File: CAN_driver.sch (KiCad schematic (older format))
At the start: 12 parts, among them J4 DB9_Female, U3 ADM3053

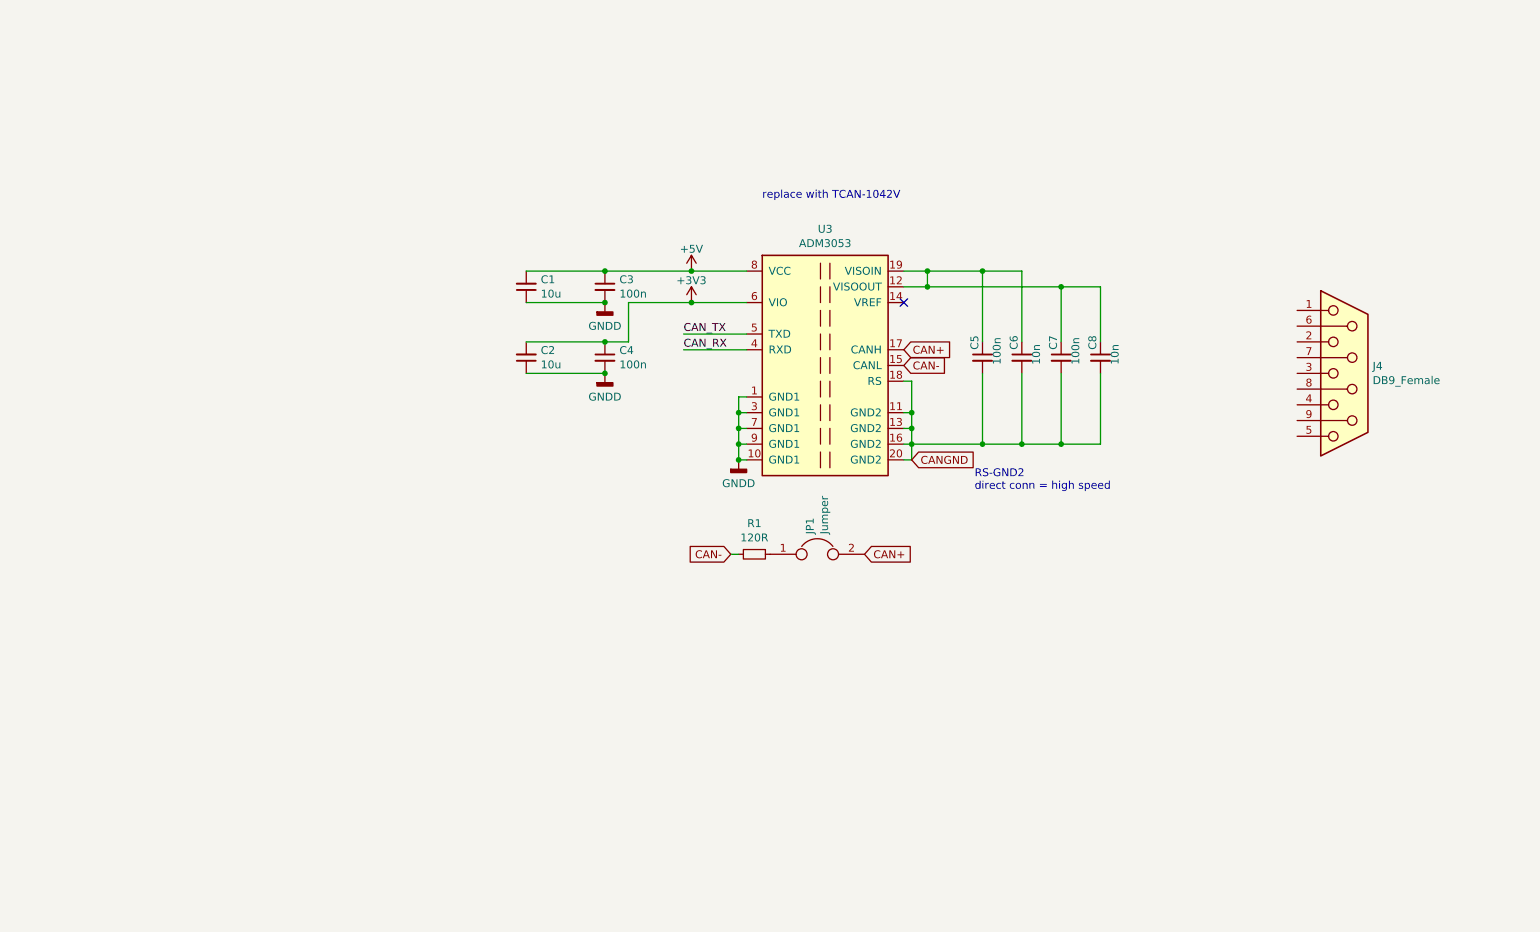
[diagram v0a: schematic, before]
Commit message: added vcu pinout, still lots needs doing
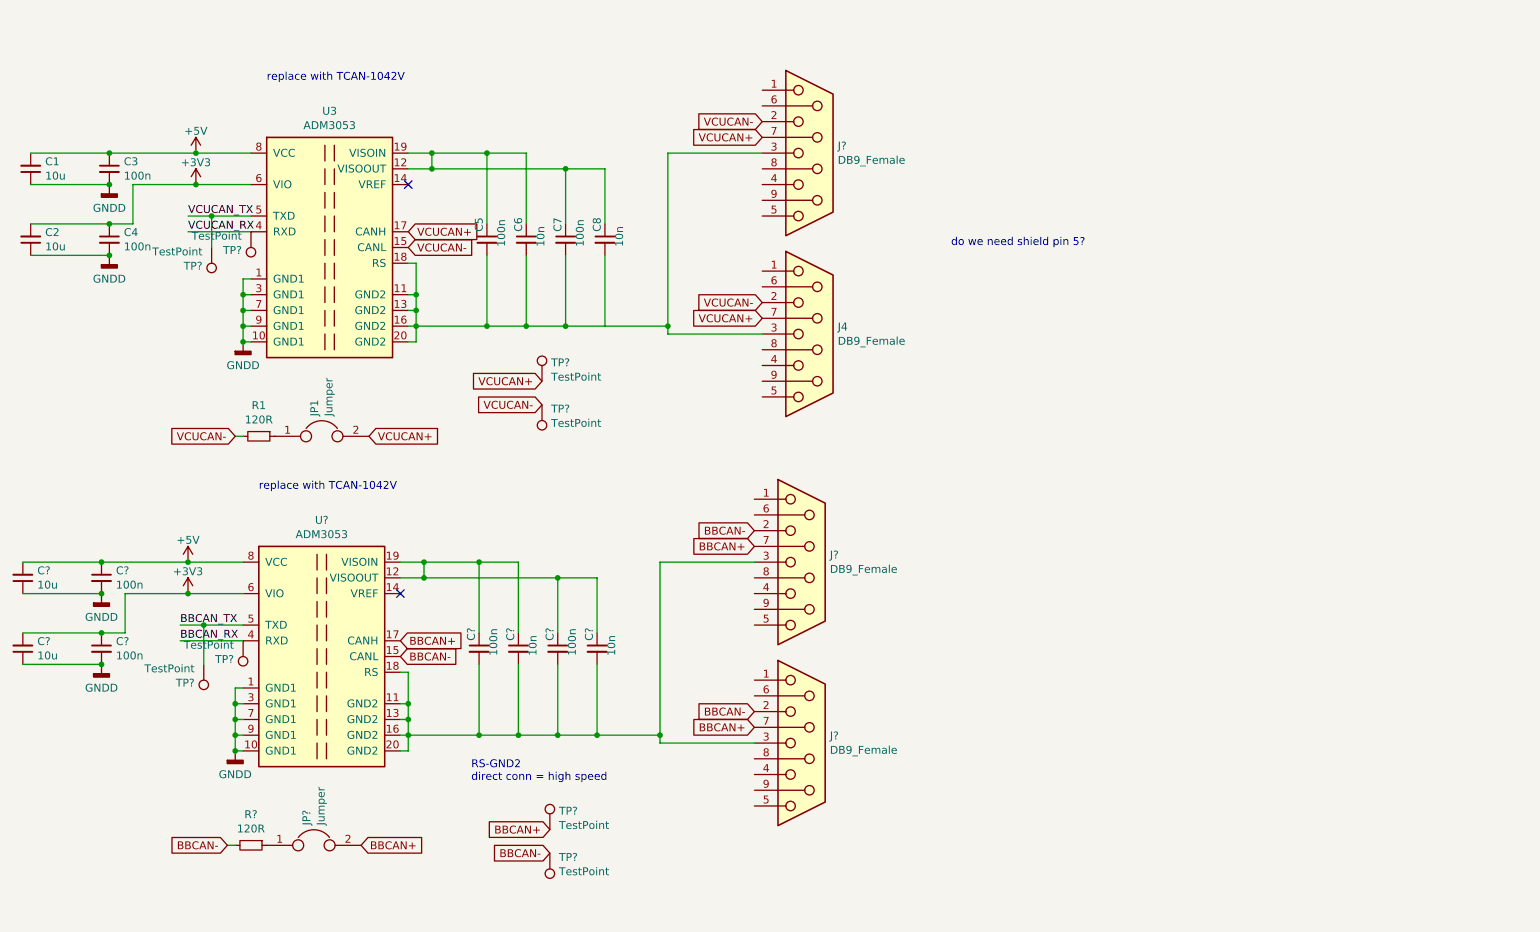
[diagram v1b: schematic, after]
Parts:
- added C? (x4): 100n, symbol Device:C_Small
- added C? (x2): 10u, symbol Device:C_Small
- added C? (x2): 10n, symbol Device:C_Small
- added J? (x3): DB9_Female, symbol Connector:DB9_Female
- added JP?: Jumper, symbol Device:Jumper
- added R?: 120R, symbol Device:R_Small
- added TP? (x8): TestPoint, symbol Connector:TestPoint
- added U?: ADM3053, Package_SO:SOIC-20W_7.5x12.8mm_P1.27mm, symbol Interface_CAN_LIN:ADM3053
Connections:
- net CAN+ is gone; now on net VCUCAN+: JP1.2, U3.17 (CANH)
- net CAN- is gone; now on net VCUCAN-: R1.2, U3.15 (CANL)
- net CANGND is gone; now on an unnamed net: C5.2, C6.2, C7.2, C8.2, U3.11 (GND2), U3.13 (GND2), U3.16 (GND2), U3.18 (RS), U3.20 (GND2)
- net +3V3: now also C?.1, C?.2, U?.6 (VIO)
- net +5V: now also C?.1, C?.2, U?.8 (VCC)
- net GNDD: now also C?.1, C?.1, C?.2, C?.2, U?.1 (GND1), U?.10 (GND1), U?.3 (GND1), U?.7 (GND1), U?.9 (GND1)
- net VCUCAN-: now reaches J4.2
- net VCUCAN-: now also J?.2, TP?.1
- net at J4.3: now also J?.3
- net VCUCAN+: now reaches J4.7
- net VCUCAN+: now also J?.7, TP?.1
- net CAN_RX renamed VCUCAN_RX
- net VCUCAN_RX: now also TP?.1
- net CAN_TX renamed VCUCAN_TX
- net VCUCAN_TX: now also TP?.1
- new net: C?.2, C?.2, C?.2, C?.2, J?.3, J?.3, U?.11 (GND2), U?.13 (GND2), U?.16 (GND2), U?.18 (RS), U?.20 (GND2)
- new net: C?.1, C?.1, C?.1, C?.1, U?.12 (VISOOUT), U?.19 (VISOIN)
- new net: JP?.1, R?.1
- new net BBCAN+: J?.7, J?.7, JP?.2, TP?.1, U?.17 (CANH)
- new net BBCAN-: J?.2, J?.2, R?.2, TP?.1, U?.15 (CANL)
- new net BBCAN_RX: TP?.1, U?.4 (RXD)
- new net BBCAN_TX: TP?.1, U?.5 (TXD)
- no-connect marks 1 -> 2
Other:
- note added: "do we need shield pin 5?"
- moved on the sheet: C1, C2, C3, C4, C5, C6, C7, C8, J4, JP1, R1, U3

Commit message: added more vcu pinout, just need to route UART, figure out GPIO problem
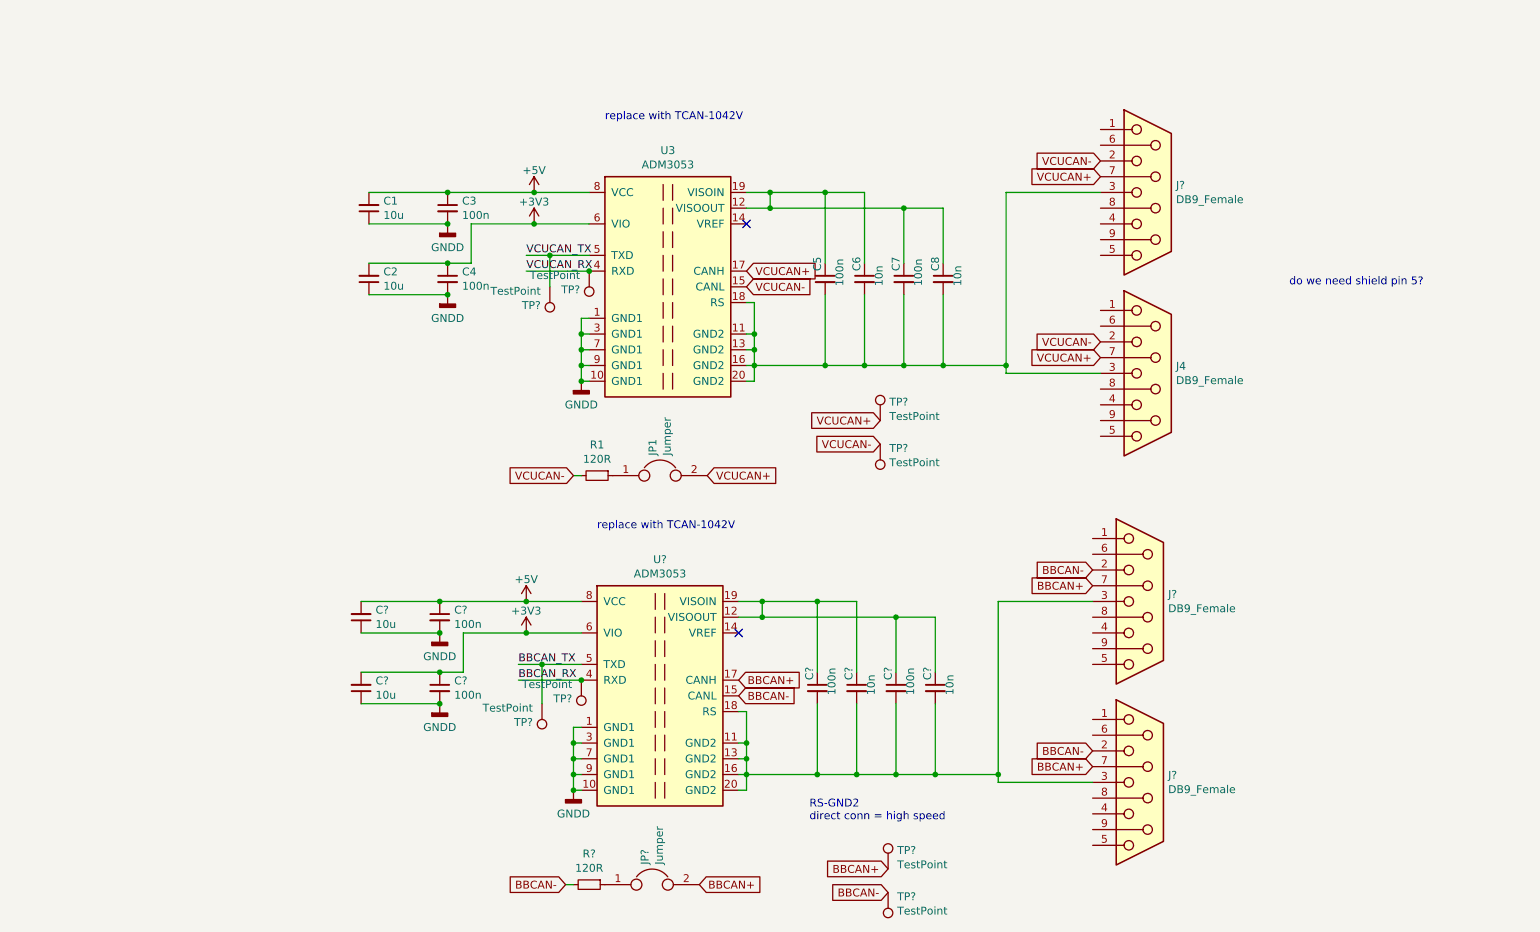
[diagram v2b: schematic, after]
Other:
- moved on the sheet: C1, C2, C3, C4, C5, C6, C7, C8, C?, J4, J?, JP1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

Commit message: added pin names vcu, rs232 mcguffins, losing hope
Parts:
- gave numbers to parts that had none: 22
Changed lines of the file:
@@
 $Descr A4 11693 8268
 encoding utf-8
-Sheet 2 2
+Sheet 2 3
 Title ""
 Date ""
@@
 P 4350 5500
 AR Path="/5E45BED6" Ref="#PWR?"  Part="1"
-AR Path="/5ED986AC/5E45BED6" Ref="#PWR?"  Part="1"
-F 0 "#PWR?" H 4350 5250 50  0001 C CNN
+AR Path="/5ED986AC/5E45BED6" Ref="#PWR0117"  Part="1"
+F 0 "#PWR0117" H 4350 5250 50  0001 C CNN
 F 1 "GNDD" H 4350 5350 50  0000 C CNN
 F 2 "" H 4350 5500 60  0000 C CNN
@@
 P 4900 4900
 AR Path="/5E45BEE7" Ref="U?"  Part="1"
-AR Path="/5ED986AC/5E45BEE7" Ref="U?"  Part="1"
-F 0 "U?" H 4900 5767 50  0000 C CNN
+AR Path="/5ED986AC/5E45BEE7" Ref="U1"  Part="1"
+F 0 "U1" H 4900 5767 50  0000 C CNN
 F 1 "ADM3053" H 4900 5676 50  0000 C CNN
 F 2 "Package_SO:SOIC-20W_7.5x12.8mm_P1.27mm" H 4900 4050 50  0001 C CNN
@@
 P 4050 4300
 AR Path="/5E45BEF9" Ref="#PWR?"  Part="1"
-AR Path="/5ED986AC/5E45BEF9" Ref="#PWR?"  Part="1"
-F 0 "#PWR?" H 4050 4150 50  0001 C CNN
+AR Path="/5ED986AC/5E45BEF9" Ref="#PWR0118"  Part="1"
+F 0 "#PWR0118" H 4050 4150 50  0001 C CNN
 F 1 "+5V" H 4050 4440 50  0000 C CNN
 F 2 "" H 4050 4300 60  0000 C CNN
@@
 P 3500 4400
 AR Path="/5E45BF0D" Ref="C?"  Part="1"
-AR Path="/5ED986AC/5E45BF0D" Ref="C?"  Part="1"
-F 0 "C?" H 3592 4446 50  0000 L CNN
+AR Path="/5ED986AC/5E45BF0D" Ref="C11"  Part="1"
+F 0 "C11" H 3592 4446 50  0000 L CNN
 F 1 "100n" H 3592 4355 50  0000 L CNN
 F 2 "" H 3500 4400 50  0001 C CNN
@@
 P 3000 4400
 AR Path="/5E45BF13" Ref="C?"  Part="1"
-AR Path="/5ED986AC/5E45BF13" Ref="C?"  Part="1"
-F 0 "C?" H 2908 4354 50  0000 R CNN
+AR Path="/5ED986AC/5E45BF13" Ref="C9"  Part="1"
+F 0 "C9" H 2908 4354 50  0000 R CNN
 F 1 "10u" H 2908 4445 50  0000 R CNN
 F 2 "" H 3000 4400 50  0001 C CNN
@@
 P 3500 4500
 AR Path="/5E45BF1A" Ref="#PWR?"  Part="1"
-AR Path="/5ED986AC/5E45BF1A" Ref="#PWR?"  Part="1"
-F 0 "#PWR?" H 3500 4250 50  0001 C CNN
+AR Path="/5ED986AC/5E45BF1A" Ref="#PWR0119"  Part="1"
+F 0 "#PWR0119" H 3500 4250 50  0001 C CNN
 F 1 "GNDD" H 3500 4350 50  0000 C CNN
 F 2 "" H 3500 4500 60  0000 C CNN
@@
 P 3500 4850
 AR Path="/5E45BF21" Ref="C?"  Part="1"
-AR Path="/5ED986AC/5E45BF21" Ref="C?"  Part="1"
-F 0 "C?" H 3592 4896 50  0000 L CNN
+AR Path="/5ED986AC/5E45BF21" Ref="C12"  Part="1"
+F 0 "C12" H 3592 4896 50  0000 L CNN
 F 1 "100n" H 3592 4805 50  0000 L CNN
 F 2 "" H 3500 4850 50  0001 C CNN
@@
 P 3000 4850
 AR Path="/5E45BF27" Ref="C?"  Part="1"
-AR Path="/5ED986AC/5E45BF27" Ref="C?"  Part="1"
-F 0 "C?" H 2908 4804 50  0000 R CNN
+AR Path="/5ED986AC/5E45BF27" Ref="C10"  Part="1"
+F 0 "C10" H 2908 4804 50  0000 R CNN
 F 1 "10u" H 2908 4895 50  0000 R CNN
 F 2 "" H 3000 4850 50  0001 C CNN
@@
 P 3500 4950
 AR Path="/5E45BF2E" Ref="#PWR?"  Part="1"
-AR Path="/5ED986AC/5E45BF2E" Ref="#PWR?"  Part="1"
-F 0 "#PWR?" H 3500 4700 50  0001 C CNN
+AR Path="/5ED986AC/5E45BF2E" Ref="#PWR0120"  Part="1"
+F 0 "#PWR0120" H 3500 4700 50  0001 C CNN
 F 1 "GNDD" H 3500 4800 50  0000 C CNN
 F 2 "" H 3500 4950 60  0000 C CNN
@@
 P 5900 4850
 AR Path="/5E45BF37" Ref="C?"  Part="1"
-AR Path="/5ED986AC/5E45BF37" Ref="C?"  Part="1"
-F 0 "C?" V 5850 4900 50  0000 L CNN
+AR Path="/5ED986AC/5E45BF37" Ref="C13"  Part="1"
+F 0 "C13" V 5850 4900 50  0000 L CNN
 F 1 "100n" V 5992 4805 50  0000 L CNN
 F 2 "" H 5900 4850 50  0001 C CNN
@@
 P 6150 4850
 AR Path="/5E45BF3D" Ref="C?"  Part="1"
-AR Path="/5ED986AC/5E45BF3D" Ref="C?"  Part="1"
-F 0 "C?" V 6100 4900 50  0000 L CNN
+AR Path="/5ED986AC/5E45BF3D" Ref="C14"  Part="1"
+F 0 "C14" V 6100 4900 50  0000 L CNN
 F 1 "10n" V 6242 4805 50  0000 L CNN
 F 2 "" H 6150 4850 50  0001 C CNN
@@
 P 6400 4850
 AR Path="/5E45BF45" Ref="C?"  Part="1"
-AR Path="/5ED986AC/5E45BF45" Ref="C?"  Part="1"
-F 0 "C?" V 6350 4900 50  0000 L CNN
+AR Path="/5ED986AC/5E45BF45" Ref="C15"  Part="1"
+F 0 "C15" V 6350 4900 50  0000 L CNN
 F 1 "100n" V 6492 4805 50  0000 L CNN
 F 2 "" H 6400 4850 50  0001 C CNN
@@
 P 6650 4850
 AR Path="/5E45BF4B" Ref="C?"  Part="1"
-AR Path="/5ED986AC/5E45BF4B" Ref="C?"  Part="1"
-F 0 "C?" V 6600 4900 50  0000 L CNN
+AR Path="/5ED986AC/5E45BF4B" Ref="C16"  Part="1"
+F 0 "C16" V 6600 4900 50  0000 L CNN
 F 1 "10n" V 6742 4805 50  0000 L CNN
 F 2 "" H 6650 4850 50  0001 C CNN
@@
 P 4450 6100
 AR Path="/5E45BF53" Ref="R?"  Part="1"
-AR Path="/5ED986AC/5E45BF53" Ref="R?"  Part="1"
-F 0 "R?" V 4254 6100 50  0000 C CNN
+AR Path="/5ED986AC/5E45BF53" Ref="R2"  Part="1"
+F 0 "R2" V 4254 6100 50  0000 C CNN
 F 1 "120R" V 4345 6100 50  0000 C CNN
 F 2 "" H 4450 6100 50  0001 C CNN
@@
 P 4850 6100
 AR Path="/5E45BF5C" Ref="JP?"  Part="1"
-AR Path="/5ED986AC/5E45BF5C" Ref="JP?"  Part="1"
-F 0 "JP?" V 4804 6227 50  0000 L CNN
+AR Path="/5ED986AC/5E45BF5C" Ref="JP2"  Part="1"
+F 0 "JP2" V 4804 6227 50  0000 L CNN
 F 1 "Jumper" V 4895 6227 50  0000 L CNN
 F 2 "" H 4850 6100 50  0001 C CNN
@@
 P 7950 5450
 AR Path="/5E45BF84" Ref="J?"  Part="1"
-AR Path="/5ED986AC/5E45BF84" Ref="J?"  Part="1"
-F 0 "J?" H 8130 5496 50  0000 L CNN
+AR Path="/5ED986AC/5E45BF84" Ref="J6"  Part="1"
+F 0 "J6" H 8130 5496 50  0000 L CNN
 F 1 "DB9_Female" H 8130 5405 50  0000 L CNN
 F 2 "" H 7950 5450 50  0001 C CNN
@@
 P 8000 1700
 AR Path="/5E494055" Ref="J?"  Part="1"
-AR Path="/5ED986AC/5E494055" Ref="J?"  Part="1"
-F 0 "J?" H 8180 1746 50  0000 L CNN
+AR Path="/5ED986AC/5E494055" Ref="J7"  Part="1"
+F 0 "J7" H 8180 1746 50  0000 L CNN
 F 1 "DB9_Female" H 8180 1655 50  0000 L CNN
 F 2 "" H 8000 1700 50  0001 C CNN
@@
 P 7950 4300
 AR Path="/5E49766F" Ref="J?"  Part="1"
-AR Path="/5ED986AC/5E49766F" Ref="J?"  Part="1"
-F 0 "J?" H 8130 4346 50  0000 L CNN
+AR Path="/5ED986AC/5E49766F" Ref="J5"  Part="1"
+F 0 "J5" H 8130 4346 50  0000 L CNN
 F 1 "DB9_Female" H 8130 4255 50  0000 L CNN
 F 2 "" H 7950 4300 50  0001 C CNN
@@
 P 4050 4500
 AR Path="/5E45BEE0" Ref="#PWR?"  Part="1"
-AR Path="/5ED986AC/5E45BEE0" Ref="#PWR?"  Part="1"
-F 0 "#PWR?" H 4050 4350 50  0001 C CNN
+AR Path="/5ED986AC/5E45BEE0" Ref="#PWR0121"  Part="1"
+F 0 "#PWR0121" H 4050 4350 50  0001 C CNN
 F 1 "+3V3" H 4050 4640 50  0000 C CNN
 F 2 "" H 4050 4500 60  0000 C CNN
@@
 do we need shield pin 5?
 $Comp
-L Connector:TestPoint TP?
+L Connector:TestPoint TP20
 U 1 1 5E97B50B
 P 6300 3150
-F 0 "TP?" H 6358 3268 50  0000 L CNN
+F 0 "TP20" H 6358 3268 50  0000 L CNN
 F 1 "TestPoint" H 6358 3177 50  0000 L CNN
 F 2 "" H 6500 3150 50  0001 C CNN
@@
 $EndComp
 $Comp
-L Connector:TestPoint TP?
+L Connector:TestPoint TP21
 U 1 1 5E981100
 P 6300 3300
-F 0 "TP?" H 6242 3326 50  0000 R CNN
+F 0 "TP21" H 6242 3326 50  0000 R CNN
 F 1 "TestPoint" H 6242 3417 50  0000 R CNN
 F 2 "" H 6500 3300 50  0001 C CNN
@@
 $EndComp
 $Comp
-L Connector:TestPoint TP?
+L Connector:TestPoint TP22
 U 1 1 5E993F56
 P 6350 6000
-F 0 "TP?" H 6408 6118 50  0000 L CNN
+F 0 "TP22" H 6408 6118 50  0000 L CNN
 F 1 "TestPoint" H 6408 6027 50  0000 L CNN
 F 2 "" H 6550 6000 50  0001 C CNN
@@
 $EndComp
 $Comp
-L Connector:TestPoint TP?
+L Connector:TestPoint TP23
 U 1 1 5E993F5C
 P 6350 6150
-F 0 "TP?" H 6292 6176 50  0000 R CNN
+F 0 "TP23" H 6292 6176 50  0000 R CNN
 F 1 "TestPoint" H 6292 6267 50  0000 R CNN
 F 2 "" H 6550 6150 50  0001 C CNN
@@
 VCUCAN-
 $Comp
-L Connector:TestPoint TP?
+L Connector:TestPoint TP19
 U 1 1 5E9B44E1
 P 4450 2200
-F 0 "TP?" H 4508 2318 50  0000 L CNN
+F 0 "TP19" H 4508 2318 50  0000 L CNN
 F 1 "TestPoint" H 4508 2227 50  0000 L CNN
 F 2 "" H 4650 2200 50  0001 C CNN
@@
 $EndComp
 $Comp
-L Connector:TestPoint TP?
+L Connector:TestPoint TP17
 U 1 1 5E9B81B1
 P 4200 2300
-F 0 "TP?" H 4258 2418 50  0000 L CNN
+F 0 "TP17" H 4258 2418 50  0000 L CNN
 F 1 "TestPoint" H 4258 2327 50  0000 L CNN
 F 2 "" H 4400 2300 50  0001 C CNN
@@
 	4200 2100 4450 2100
 $Comp
-L Connector:TestPoint TP?
+L Connector:TestPoint TP18
 U 1 1 5E9C42B3
 P 4400 4800
-F 0 "TP?" H 4458 4918 50  0000 L CNN
+F 0 "TP18" H 4458 4918 50  0000 L CNN
 F 1 "TestPoint" H 4458 4827 50  0000 L CNN
 F 2 "" H 4600 4800 50  0001 C CNN
@@
 $EndComp
 $Comp
-L Connector:TestPoint TP?
+L Connector:TestPoint TP16
 U 1 1 5E9C8FEE
 P 4150 4950
-F 0 "TP?" H 4208 5068 50  0000 L CNN
+F 0 "TP16" H 4208 5068 50  0000 L CNN
 F 1 "TestPoint" H 4208 4977 50  0000 L CNN
 F 2 "" H 4350 4950 50  0001 C CNN

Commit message: sleep isn't real. Fixed pins. DAC hell. Nearly done on schematic.
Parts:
- added JP? (x2): Jumper, symbol Device:Jumper
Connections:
- net BBCAN+: now also JP?.2
- net BBCAN-: now also JP?.2
- net VCUCAN+: now also JP?.1
- net VCUCAN-: now also JP?.1
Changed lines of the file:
@@
 Connection ~ 4450 2200
 Connection ~ 6700 2800
+Text GLabel 9900 3850 2    50   Input ~ 0
+VCUCAN+
+$Comp
+L Device:Jumper JP?
+U 1 1 5F7EB443
+P 9900 4150
+AR Path="/5F7EB443" Ref="JP?"  Part="1"
+AR Path="/5ED986AC/5F7EB443" Ref="JP?"  Part="1"
+F 0 "JP?" V 9854 4277 50  0000 L CNN
+F 1 "Jumper" V 9945 4277 50  0000 L CNN
+F 2 "" H 9900 4150 50  0001 C CNN
+F 3 "~" H 9900 4150 50  0001 C CNN
+	1    9900 4150
+	0    1    1    0
+$EndComp
+Text GLabel 9300 3850 0    50   Input ~ 0
+VCUCAN-
+$Comp
+L Device:Jumper JP?
+U 1 1 5F801A87
+P 9300 4150
+AR Path="/5F801A87" Ref="JP?"  Part="1"
+AR Path="/5ED986AC/5F801A87" Ref="JP?"  Part="1"
+F 0 "JP?" V 9254 4277 50  0000 L CNN
+F 1 "Jumper" V 9345 4277 50  0000 L CNN
+F 2 "" H 9300 4150 50  0001 C CNN
+F 3 "~" H 9300 4150 50  0001 C CNN
+	1    9300 4150
+	0    1    1    0
+$EndComp
+Text GLabel 9900 4450 2    50   Input ~ 0
+BBCAN+
+Text GLabel 9300 4450 0    50   Input ~ 0
+BBCAN-
 $EndSCHEMATC
